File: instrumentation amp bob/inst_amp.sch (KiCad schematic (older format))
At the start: 26 parts, among them J1 Conn_01x03, J2 Conn_01x03, J3 Conn_01x05, U1 AD8429, U2 OP1177

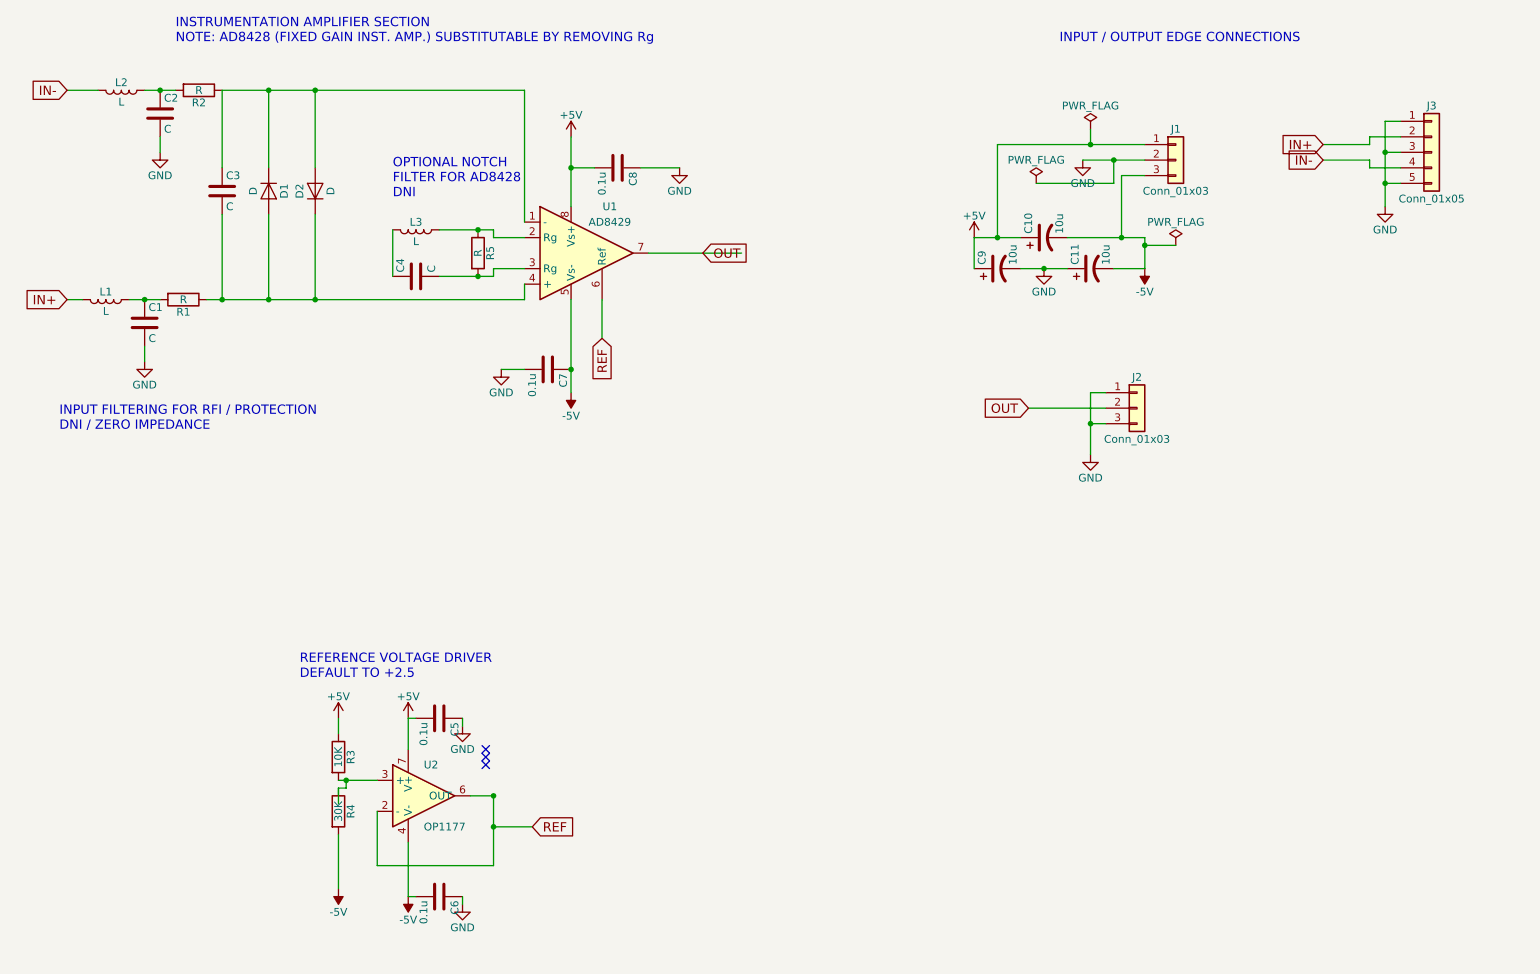
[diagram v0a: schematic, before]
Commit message: incorporated schematic changes from peer review
power PI filter
test points
reference voltage conector
reference voltage LP filter
power reverse bias protection
power presense led
gain pot
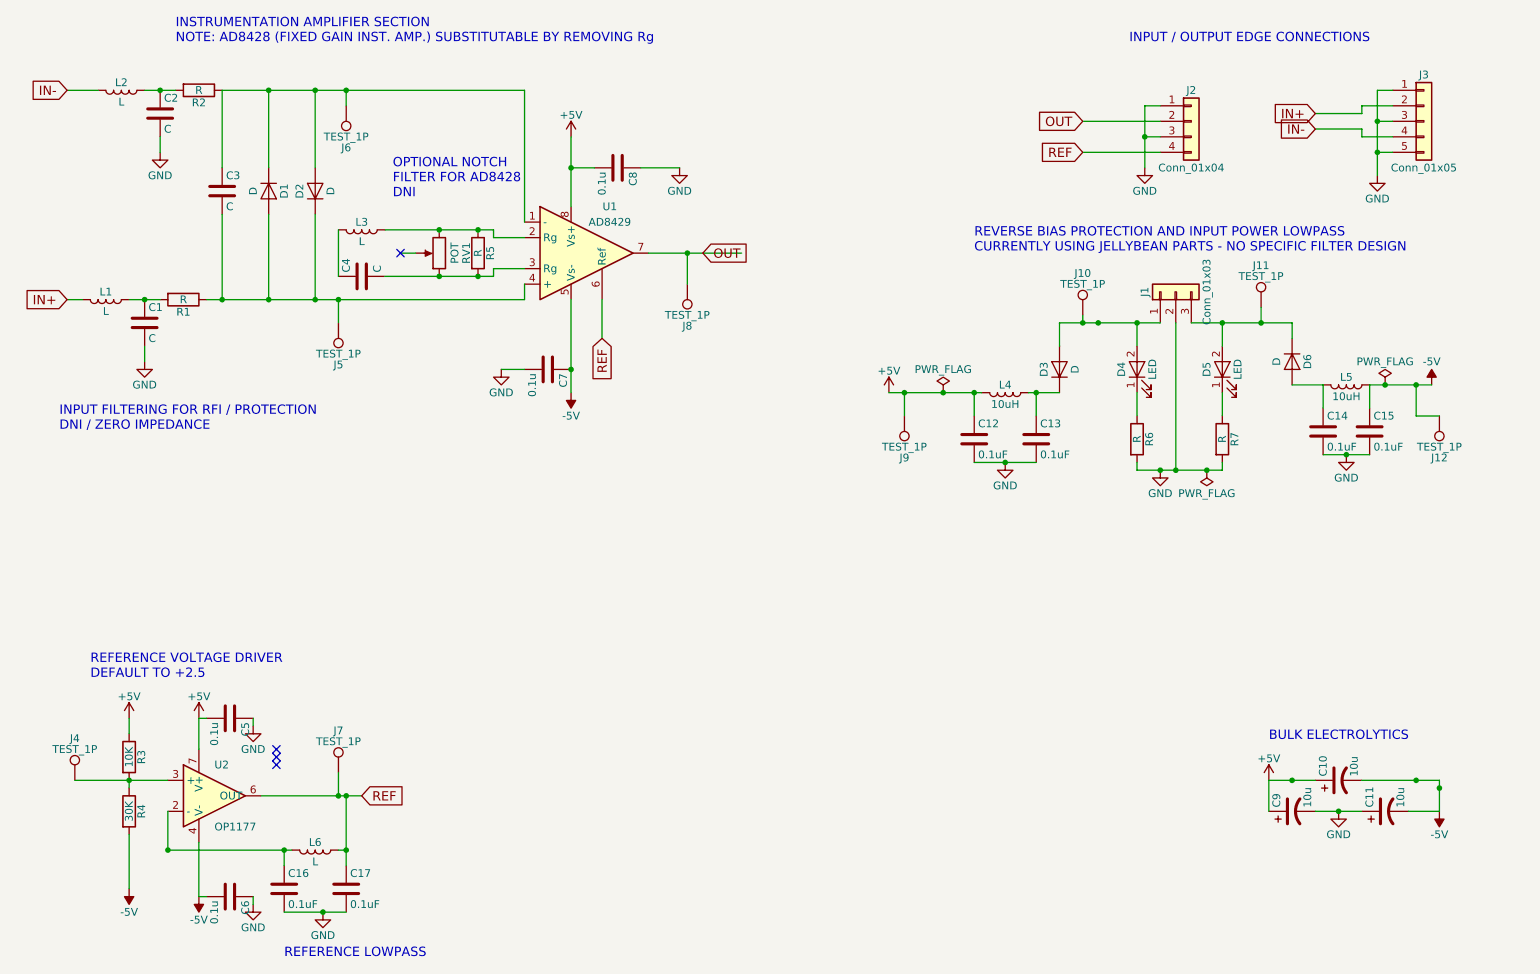
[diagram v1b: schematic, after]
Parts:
- removed J2: Conn_01x03, Pin_Headers:Pin_Header_Angled_1x03_Pitch2.54mm, symbol Conn_01x03
- added C12, C13, C14, C15, C16, C17: 0.1uF, Capacitors_SMD:C_0805_HandSoldering, symbol C
- added D3, D6: D, Diodes_SMD:D_0805, symbol D
- added D4, D5: LED, Diodes_SMD:D_0805, symbol LED
- added J10, J11, J12, J4, J5, J6, J7, J8, J9: TEST_1P, Measurement_Points:Measurement_Point_Round-SMD-Pad_Big, symbol TEST_1P
- added J2: Conn_01x04, Pin_Headers:Pin_Header_Angled_1x04_Pitch2.54mm, symbol Conn_01x04
- added L4, L5: 10uH, Inductors_SMD:L_0805_HandSoldering, symbol L
- added L6: L, Inductors_SMD:L_0805_HandSoldering, symbol L
- added R6, R7: R, Resistors_SMD:R_0805_HandSoldering, symbol R
- added RV1: POT, symbol POT
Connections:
- net +5V: now also C12.1, J9.1, L4.2; no longer J1.1 (Pin_1)
- net -5V: now also C15.1, J12.1, L5.1; no longer J1.3 (Pin_3)
- net GND: now also C12.2, C13.2, C14.2, C15.2, C16.2, C17.2, J2.1 (Pin_1), J2.3 (Pin_3), R6.2, R7.2
- net OUT: now also J2.2 (Pin_2), J8.1
- net REF: now also C17.1, J2.4 (Pin_4), J7.1, L6.1; no longer U2.2 (-)
- net at C3.1, D1.1 (K), D2.2 (A)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: now also J6.1
- net at L3.1, R5.1, U1.2 (Rg): now also RV1.3
- net at C4.2, R5.2, U1.3 (Rg): now also RV1.1
- net at C3.2, D1.2 (A), D2.1 (K)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: now also J5.1
- net at R3.2, R4.1, U2.3 (+): now also J4.1
- new net: D3.2 (A), D4.2 (A), J1.1 (Pin_1), J10.1
- new net: D5.2 (A), D6.1 (K), J1.3 (Pin_3), J11.1
- new net: C16.1, L6.2, U2.2 (-)
- new net: C13.1, D3.1 (K), L4.1
- new net: C14.1, D6.2 (A), L5.2
- new net: D4.1 (K), R6.1
- new net: D5.1 (K), R7.1
- no-connect marks 3 -> 4
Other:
- note added: "BULK ELECTROLYTICS"
- note added: "REFERENCE LOWPASS"
- note added: "REVERSE BIAS PROTECTION AND INPUT POWER LOWPASS\nCURRENTLY USING JELLYBEAN PARTS - NO SPECIFIC FILTER DESIGN"
- moved on the sheet: C10, C11, C4, C5, C6, C9, J1, J3, L3, R3, R4, U2

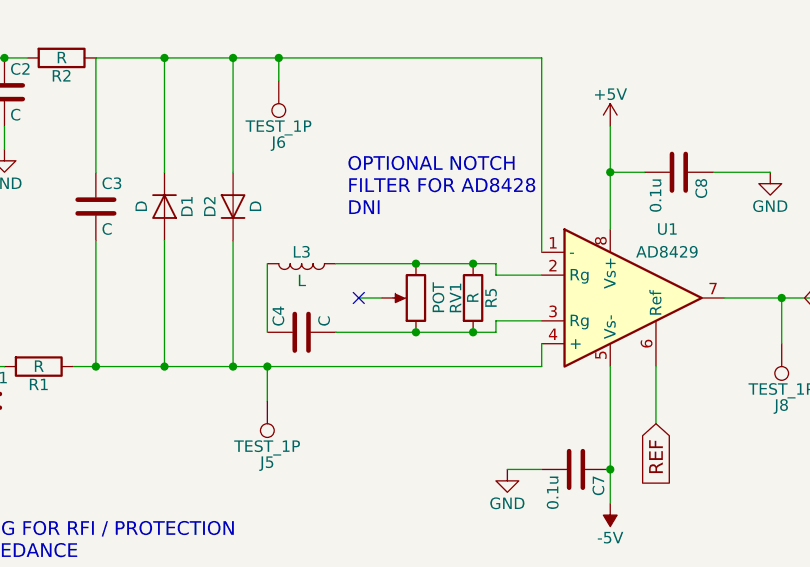
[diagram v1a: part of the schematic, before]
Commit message: selected pot footprint, fixed pot connection bug
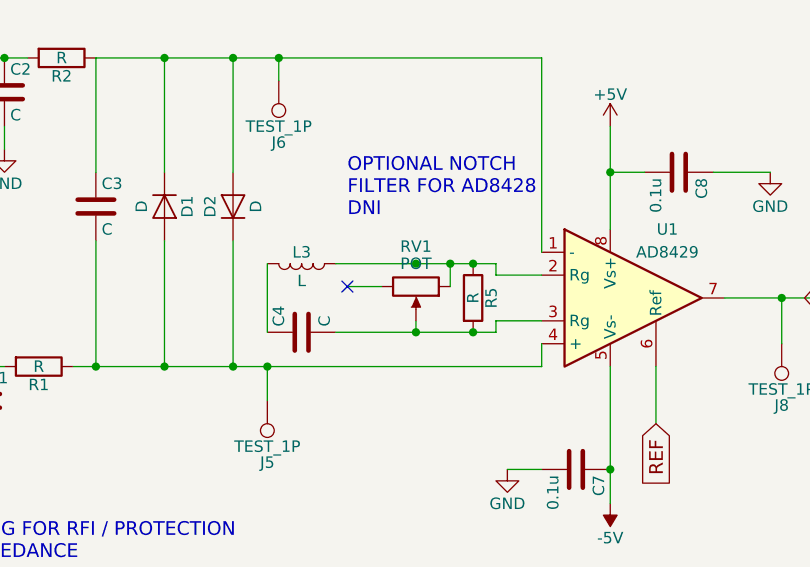
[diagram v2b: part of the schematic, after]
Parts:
- RV1: footprint (none) -> Potentiometers:Potentiometer_Trimmer_Bourns_PV36W
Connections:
- net at L3.1, R5.1, U1.2 (Rg): now also RV1.1; no longer RV1.3
- net at C4.2, R5.2, U1.3 (Rg): now also RV1.2; no longer RV1.1
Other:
- moved on the sheet: RV1
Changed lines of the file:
@@
 L POT RV1
 U 1 1 59F30629
-P 3500 2450
-F 0 "RV1" V 3325 2450 50  0000 C CNN
-F 1 "POT" V 3400 2450 50  0000 C CNN
-F 2 "" H 3500 2450 50  0001 C CNN
-F 3 "" H 3500 2450 50  0001 C CNN
-	1    3500 2450
-	-1   0    0    1
+P 3500 2400
+F 0 "RV1" V 3325 2400 50  0000 C CNN
+F 1 "POT" V 3400 2400 50  0000 C CNN
+F 2 "Potentiometers:Potentiometer_Trimmer_Bourns_PV36W" H 3500 2400 50  0001 C CNN
+F 3 "" H 3500 2400 50  0001 C CNN
+	1    3500 2400
+	0    1    1    0
 $EndComp
 Connection ~ 3500 2300
@@
 Wire Wire Line
 	8800 2800 8800 2900
-NoConn ~ 3250 2450
-Wire Wire Line
-	3350 2450 3250 2450
+NoConn ~ 3200 2400
 Wire Wire Line
 	1150 5850 1750 5850
@@
 Wire Wire Line
 	1500 5900 1500 5850
+Wire Wire Line
+	3650 2300 3650 2400
+Wire Wire Line
+	3500 2550 3500 2600
+Connection ~ 3650 2300
+Wire Wire Line
+	3350 2400 3200 2400
 $EndSCHEMATC

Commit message: incorporated review comments to layout
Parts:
- C10, C11, C9: footprint Capacitors_SMD:CP_Elec_6.3x7.7 -> Capacitors_THT:CP_Radial_D5.0mm_P2.00mm
- J10, J11, J12, J4, J5, J6, J7, J8, J9: footprint Measurement_Points:Measurement_Point_Round-SMD-Pad_Big -> Measurement_Points:Measurement_Point_Round-SMD-Pad_Small
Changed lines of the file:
@@
 $EndComp
 $Comp
-L -5V #PWR4
+L -5V #PWR2
 U 1 1 59F0CCD0
 P 1500 6550
-F 0 "#PWR4" H 1500 6650 50  0001 C CNN
+F 0 "#PWR2" H 1500 6650 50  0001 C CNN
 F 1 "-5V" H 1500 6700 50  0000 C CNN
 F 2 "" H 1500 6550 50  0001 C CNN
@@
 $EndComp
 $Comp
-L -5V #PWR17
+L -5V #PWR23
 U 1 1 59F12A5C
 P 9950 6050
-F 0 "#PWR17" H 9950 6150 50  0001 C CNN
+F 0 "#PWR23" H 9950 6150 50  0001 C CNN
 F 1 "-5V" H 9950 6200 50  0000 C CNN
 F 2 "" H 9950 6050 50  0001 C CNN
@@
 F 0 "C10" H 9325 5950 50  0000 L CNN
 F 1 "10u" H 9325 5750 50  0000 L CNN
-F 2 "Capacitors_SMD:CP_Elec_6.3x7.7" H 9300 5850 50  0001 C CNN
+F 2 "Capacitors_THT:CP_Radial_D5.0mm_P2.00mm" H 9300 5850 50  0001 C CNN
 F 3 "" H 9300 5850 50  0001 C CNN
 	1    9300 5850
@@
 F 0 "C9" H 9025 6150 50  0000 L CNN
 F 1 "10u" H 9025 5950 50  0000 L CNN
-F 2 "Capacitors_SMD:CP_Elec_6.3x7.7" H 9000 6050 50  0001 C CNN
+F 2 "Capacitors_THT:CP_Radial_D5.0mm_P2.00mm" H 9000 6050 50  0001 C CNN
 F 3 "" H 9000 6050 50  0001 C CNN
 	1    9000 6050
@@
 F 0 "C11" H 9625 6150 50  0000 L CNN
 F 1 "10u" H 9625 5950 50  0000 L CNN
-F 2 "Capacitors_SMD:CP_Elec_6.3x7.7" H 9600 6050 50  0001 C CNN
+F 2 "Capacitors_THT:CP_Radial_D5.0mm_P2.00mm" H 9600 6050 50  0001 C CNN
 F 3 "" H 9600 6050 50  0001 C CNN
 	1    9600 6050
@@
 $EndComp
 $Comp
-L -5V #PWR23
+L -5V #PWR22
 U 1 1 59F25EC1
 P 9900 3300
-F 0 "#PWR23" H 9900 3400 50  0001 C CNN
+F 0 "#PWR22" H 9900 3400 50  0001 C CNN
 F 1 "-5V" H 9900 3450 50  0000 C CNN
 F 2 "" H 9900 3300 50  0001 C CNN
@@
 F 0 "J4" H 1150 6120 50  0000 C CNN
 F 1 "TEST_1P" H 1150 6050 50  0000 C CNN
-F 2 "Measurement_Points:Measurement_Point_Round-SMD-Pad_Big" H 1350 5850 50  0001 C CNN
+F 2 "Measurement_Points:Measurement_Point_Round-SMD-Pad_Small" H 1350 5850 50  0001 C CNN
 F 3 "" H 1350 5850 50  0001 C CNN
 	1    1150 5850
@@
 F 0 "J7" H 2850 6070 50  0000 C CNN
 F 1 "TEST_1P" H 2850 6000 50  0000 C CNN
-F 2 "Measurement_Points:Measurement_Point_Round-SMD-Pad_Big" H 3050 5800 50  0001 C CNN
+F 2 "Measurement_Points:Measurement_Point_Round-SMD-Pad_Small" H 3050 5800 50  0001 C CNN
 F 3 "" H 3050 5800 50  0001 C CNN
 	1    2850 5800
@@
 F 0 "J8" H 5100 2920 50  0000 C CNN
 F 1 "TEST_1P" H 5100 2850 50  0000 C CNN
-F 2 "Measurement_Points:Measurement_Point_Round-SMD-Pad_Big" H 5300 2650 50  0001 C CNN
+F 2 "Measurement_Points:Measurement_Point_Round-SMD-Pad_Small" H 5300 2650 50  0001 C CNN
 F 3 "" H 5300 2650 50  0001 C CNN
 	1    5100 2650
@@
 F 0 "J10" H 7650 3120 50  0000 C CNN
 F 1 "TEST_1P" H 7650 3050 50  0000 C CNN
-F 2 "Measurement_Points:Measurement_Point_Round-SMD-Pad_Big" H 7850 2850 50  0001 C CNN
+F 2 "Measurement_Points:Measurement_Point_Round-SMD-Pad_Small" H 7850 2850 50  0001 C CNN
 F 3 "" H 7850 2850 50  0001 C CNN
 	1    7650 2850
@@
 F 0 "J11" H 8800 3070 50  0000 C CNN
 F 1 "TEST_1P" H 8800 3000 50  0000 C CNN
-F 2 "Measurement_Points:Measurement_Point_Round-SMD-Pad_Big" H 9000 2800 50  0001 C CNN
+F 2 "Measurement_Points:Measurement_Point_Round-SMD-Pad_Small" H 9000 2800 50  0001 C CNN
 F 3 "" H 9000 2800 50  0001 C CNN
 	1    8800 2800
@@
 F 0 "J9" H 6500 3770 50  0000 C CNN
 F 1 "TEST_1P" H 6500 3700 50  0000 C CNN
-F 2 "Measurement_Points:Measurement_Point_Round-SMD-Pad_Big" H 6700 3500 50  0001 C CNN
+F 2 "Measurement_Points:Measurement_Point_Round-SMD-Pad_Small" H 6700 3500 50  0001 C CNN
 F 3 "" H 6700 3500 50  0001 C CNN
 	1    6500 3500
@@
 F 0 "J12" H 9950 3770 50  0000 C CNN
 F 1 "TEST_1P" H 9950 3700 50  0000 C CNN
-F 2 "Measurement_Points:Measurement_Point_Round-SMD-Pad_Big" H 10150 3500 50  0001 C CNN
+F 2 "Measurement_Points:Measurement_Point_Round-SMD-Pad_Small" H 10150 3500 50  0001 C CNN
 F 3 "" H 10150 3500 50  0001 C CNN
 	1    9950 3500
@@
 F 0 "J6" H 2900 1770 50  0000 C CNN
 F 1 "TEST_1P" H 2900 1700 50  0000 C CNN
-F 2 "Measurement_Points:Measurement_Point_Round-SMD-Pad_Big" H 3100 1500 50  0001 C CNN
+F 2 "Measurement_Points:Measurement_Point_Round-SMD-Pad_Small" H 3100 1500 50  0001 C CNN
 F 3 "" H 3100 1500 50  0001 C CNN
 	1    2900 1500
@@
 F 0 "J5" H 2850 3170 50  0000 C CNN
 F 1 "TEST_1P" H 2850 3100 50  0000 C CNN
-F 2 "Measurement_Points:Measurement_Point_Round-SMD-Pad_Big" H 3050 2900 50  0001 C CNN
+F 2 "Measurement_Points:Measurement_Point_Round-SMD-Pad_Small" H 3050 2900 50  0001 C CNN
 F 3 "" H 3050 2900 50  0001 C CNN
 	1    2850 2900
